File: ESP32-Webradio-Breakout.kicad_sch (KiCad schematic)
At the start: 18 parts, among them J1 Conn_01x02, J3 RCJ-042, J4 RCJ-041, SW1 RotaryEncoder_Switch, U1 ESP32NodeMCU

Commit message: Display and Remote 8-Bit I/O Expander for I2C added
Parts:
- added DS1: WC1602A, Display:WC1602A, symbol Display_Character:WC1602A
- added R10, R8, R9: 10k, Resistor_THT:R_Axial_DIN0207_L6.3mm_D2.5mm_P10.16mm_Horizontal, symbol Device:R
- added RV1: (no value), symbol Device:R_Potentiometer
- added U3: PCF8574, Package_DIP:DIP-16_W10.16mm_LongPads, symbol Interface_Expansion:PCF8574
- C1, C2: value (none) -> 4.7 uF/50V; footprint (none) -> Capacitor_THT:CP_Radial_D6.3mm_P2.50mm
- D1: value (none) -> 1N4001; footprint (none) -> Diode_THT:D_DO-41_SOD81_P10.16mm_Horizontal
- L1: value (none) -> 8.2 uH/1.5 A/0.08 W; footprint (none) -> Inductor_SMD:L_AVX_LMLP07A7
- R4, R5: value (none) -> 22k
- R6, R7: value (none) -> 4k7
- U2: value (none) -> TSR_1-2450; footprint (none) -> Converter_DCDC:Converter_DCDC_TRACO_TSR-1_THT
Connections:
- net +5V: now also DS1.2 (VDD), R10.1, R8.1, R9.1, RV1.1, U3.16 (VDD)
- net GND: now also DS1.1 (VSS), DS1.16 (LED(-)), RV1.3, U3.1 (A0), U3.2 (A1), U3.3 (A2), U3.8 (VSS)
- new net: DS1.11 (D4), U3.9 (P4)
- new net: DS1.12 (D5), U3.10 (P5)
- new net: DS1.13 (D6), U3.11 (P6)
- new net: DS1.14 (D7), U3.12 (P7)
- new net: DS1.3 (VO), RV1.2
- new net: DS1.4 (RS), U3.6 (P2)
- new net: DS1.5 (R/W), U3.5 (P1)
- new net: DS1.6 (E), U3.4 (P0)
- new net: R10.2, U3.13 (~{INT})
- new net: R8.2, U3.14 (SCL)
- new net: R9.2, U3.15 (SDA)
- no-connect marks 19 -> 24
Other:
- moved on the sheet: C1, C2, D1, D2, J1, J3, J4, L1, R1, R2, R3, R4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

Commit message: Adding 3D Model for Potentiometer ACP-CA9-V10
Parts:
- RV1: value (none) -> R_Potentiometer; footprint (none) -> Potentiometer_THT:Potentiometer_ACP_CA9-V10_Vertical_Hole
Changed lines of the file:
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@@
       (effects (font (size 1.27 1.27)) (justify right))
     )
-    (property "Value" "" (id 1) (at 182.88 187.9599 0)
+    (property "Value" "R_Potentiometer" (id 1) (at 182.88 187.9599 0)
       (effects (font (size 1.27 1.27)) (justify right))
     )
-    (property "Footprint" "" (id 2) (at 180.34 186.69 0)
+    (property "Footprint" "Potentiometer_THT:Potentiometer_ACP_CA9-V10_Vertical_Hole" (id 2) (at 180.34 186.69 0)
       (effects (font (size 1.27 1.27)) hide)
     )
@@
       (effects (font (size 1.27 1.27)) hide)
     )
-    (property "Value" "" (id 1) (at 180.34 232.41 0))
+    (property "Value" "GND" (id 1) (at 180.34 232.41 0))
     (property "Footprint" "" (id 2) (at 180.34 227.33 0)
       (effects (font (size 1.27 1.27)) hide)

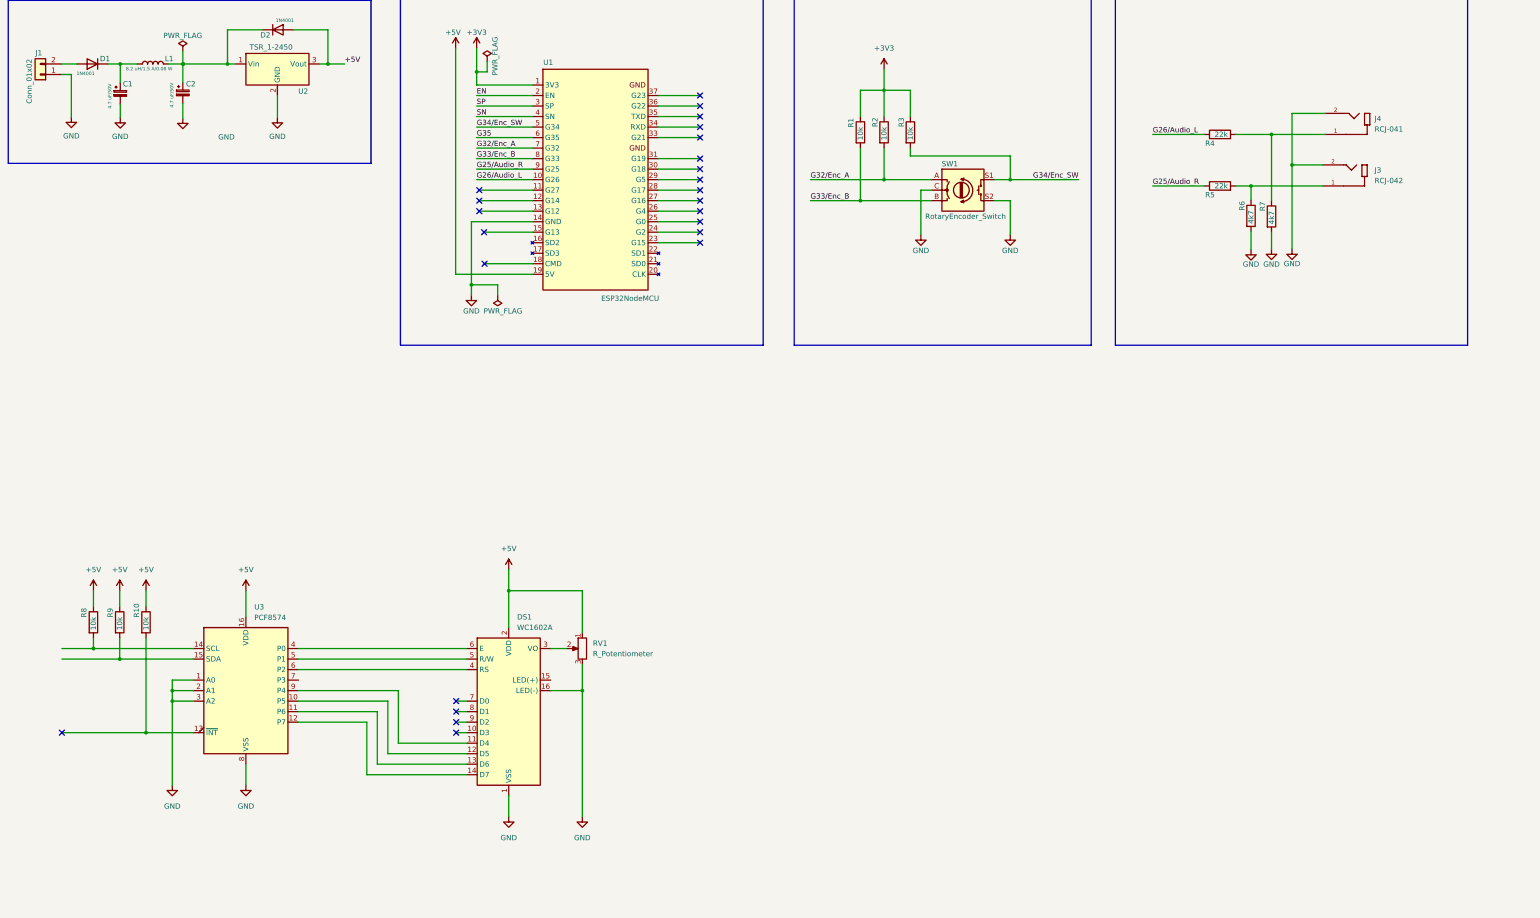
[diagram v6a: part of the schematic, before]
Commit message: Adding NPN-Transistor to switch the Backlight
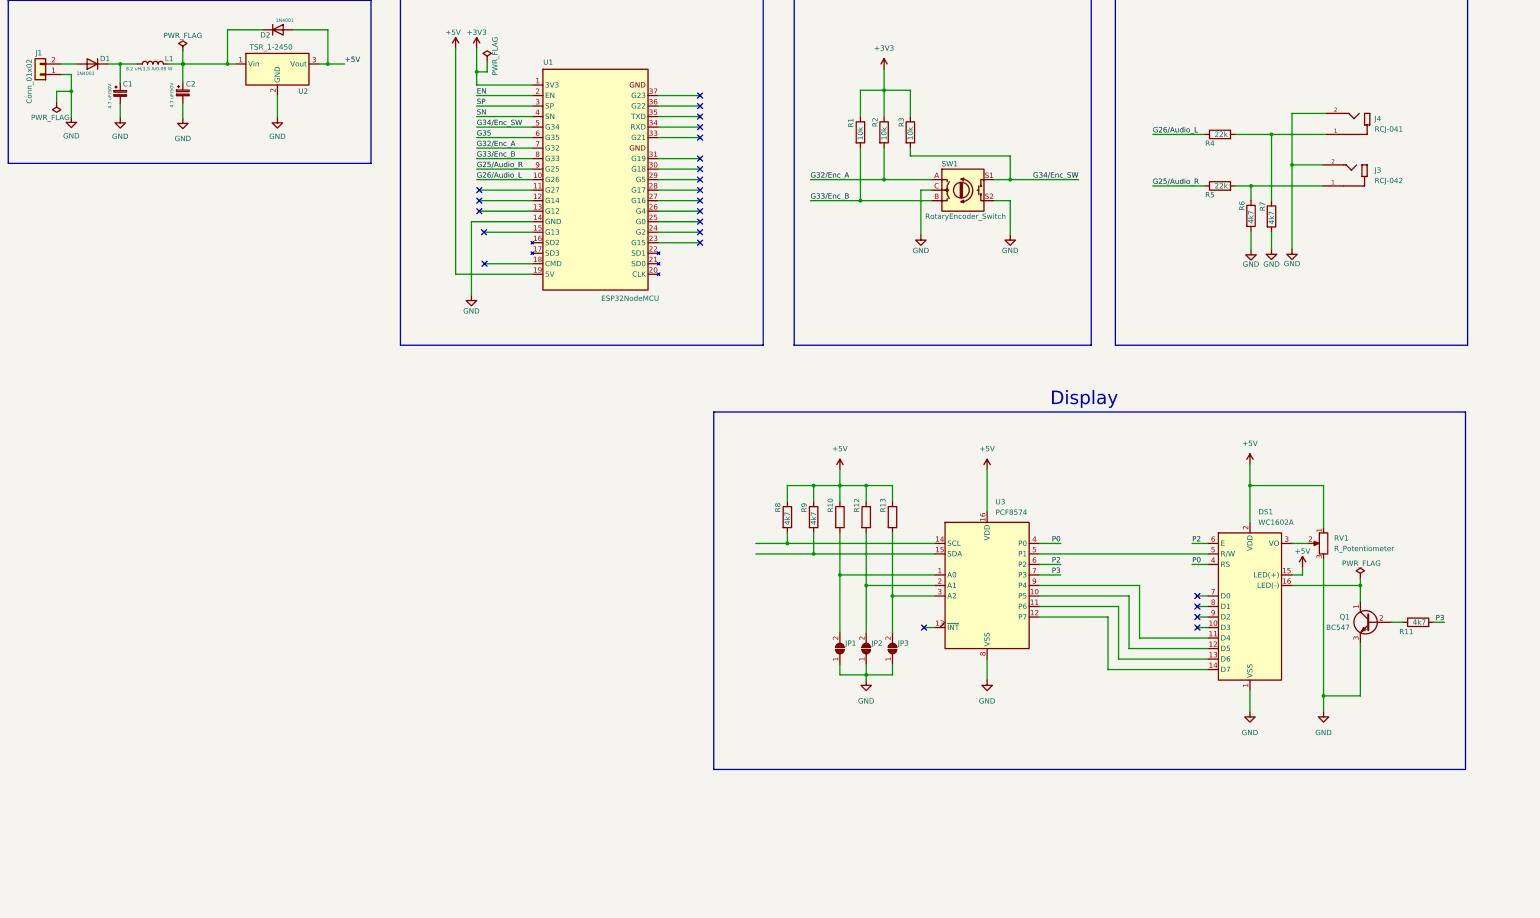
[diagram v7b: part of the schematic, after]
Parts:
- added JP1, JP2, JP3: (no value), symbol Jumper:SolderJumper_2_Open
- added Q1: BC547, Package_TO_SOT_THT:TO-92_Inline, symbol Transistor_BJT:BC547
- added R11: 4k7, Resistor_THT:R_Axial_DIN0207_L6.3mm_D2.5mm_P10.16mm_Horizontal, symbol Device:R
- added R12, R13: (no value), Resistor_THT:R_Axial_DIN0207_L6.3mm_D2.5mm_P10.16mm_Horizontal, symbol Device:R
- R10: value 10k -> (none)
- R8, R9: value 10k -> 4k7
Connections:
- net +5V: now also DS1.15 (LED(+)), R12.1, R13.1
- net GND: now also JP1.1 (A), JP2.1 (A), JP3.1 (A), Q1.3 (E); no longer DS1.16 (LED(-)), U3.1 (A0), U3.2 (A1), U3.3 (A2)
- net P0: now reaches DS1.4 (RS)
- net P0: now also U3.4 (P0); no longer U3.6 (P2)
- net P2: now reaches DS1.6 (E)
- net P2: now also U3.6 (P2); no longer U3.4 (P0)
- net at R10.2: now also U3.1 (A0), JP1.2 (B); no longer U3.13 (~{INT})
- net P3: now reaches U3.7 (P3)
- net P3: now also R11.2
- new net: DS1.16 (LED(-)), Q1.1 (C)
- new net: JP3.2 (B), R13.2, U3.3 (A2)
- new net: JP2.2 (B), R12.2, U3.2 (A1)
- new net: Q1.2 (B), R11.1
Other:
- note added: "Display"
- moved on the sheet: DS1, R8, R9, RV1, U3

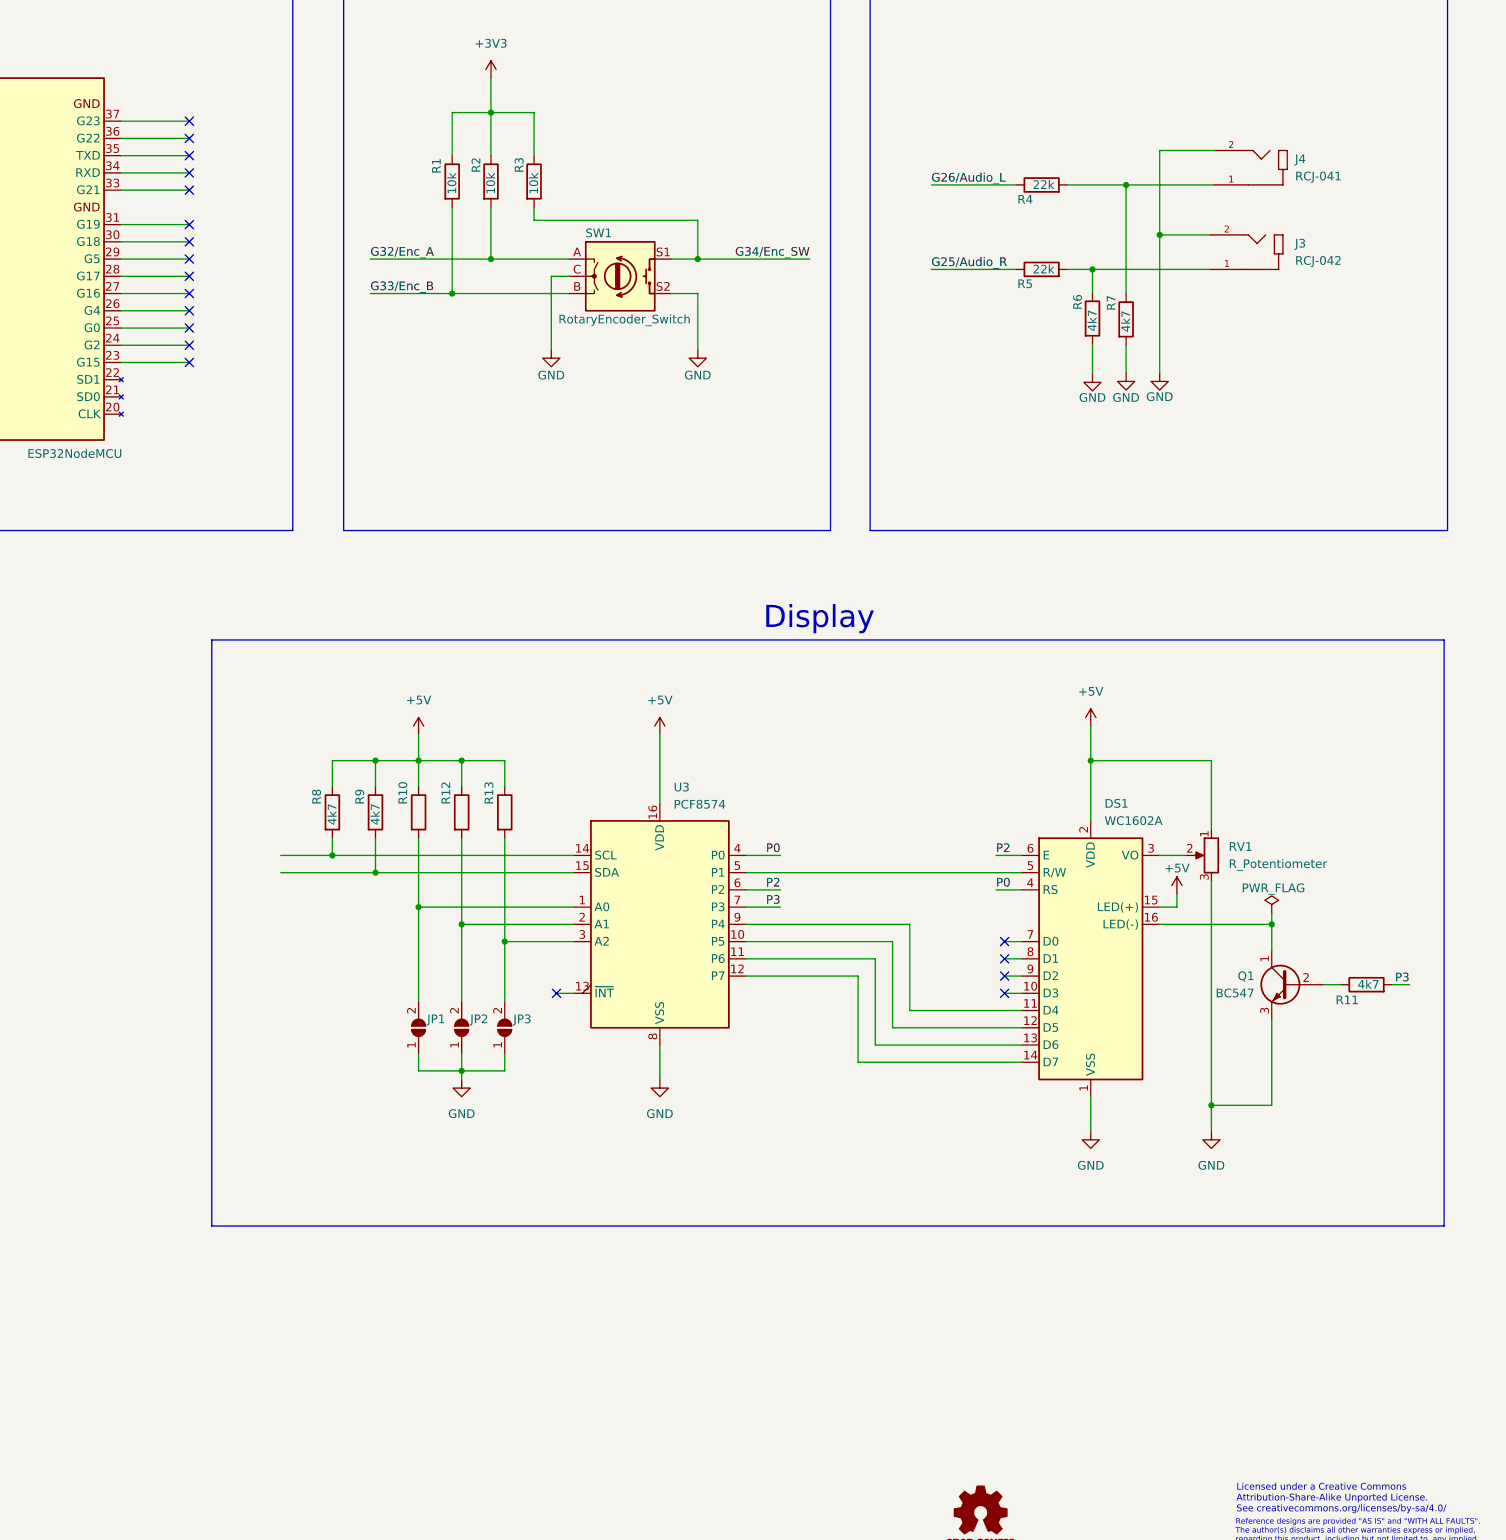
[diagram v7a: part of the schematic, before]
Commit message: adding some mounting holes and README file
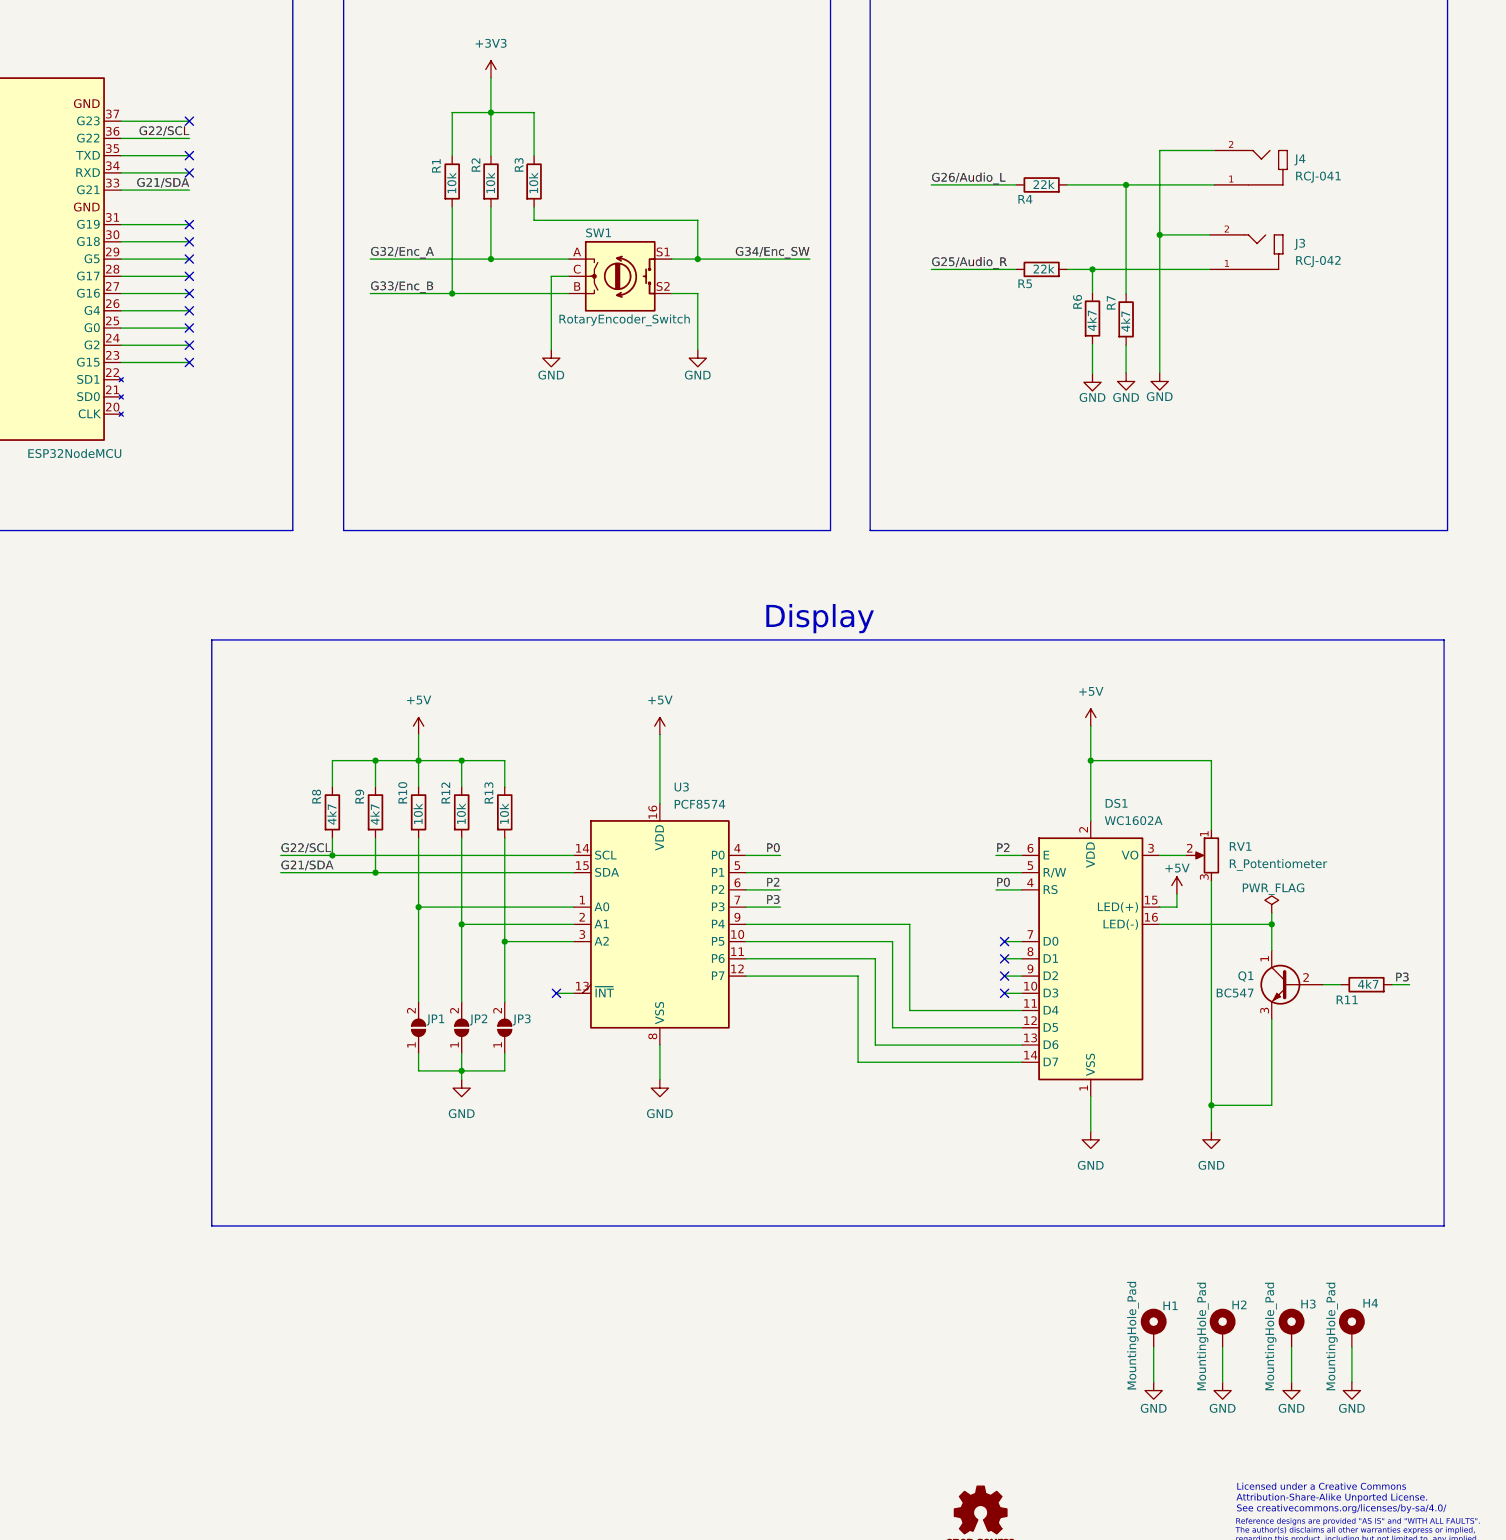
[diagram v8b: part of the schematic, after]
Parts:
- added H1, H2, H3, H4: MountingHole_Pad, MountingHole:MountingHole_3.2mm_M3_DIN965_Pad, symbol Mechanical:MountingHole_Pad
- JP1, JP2, JP3: value (none) -> SolderJumper_2_Open; footprint (none) -> Jumper:SolderJumper-2_P1.3mm_Open_TrianglePad1.0x1.5mm
- R10, R12, R13: value (none) -> 10k
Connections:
- net GND: now also H1.1, H2.1, H3.1, H4.1
- net G21/SDA: now reaches U1.33 (G21)
- net G21/SDA: now also R9.2, U3.15 (SDA)
- net G22/SCL: now reaches U1.36 (G22)
- net G22/SCL: now also R8.2, U3.14 (SCL)
- no-connect marks 24 -> 22
